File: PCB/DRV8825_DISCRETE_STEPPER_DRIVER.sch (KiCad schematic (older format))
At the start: 13 parts, among them U2 DRV8825PWPR

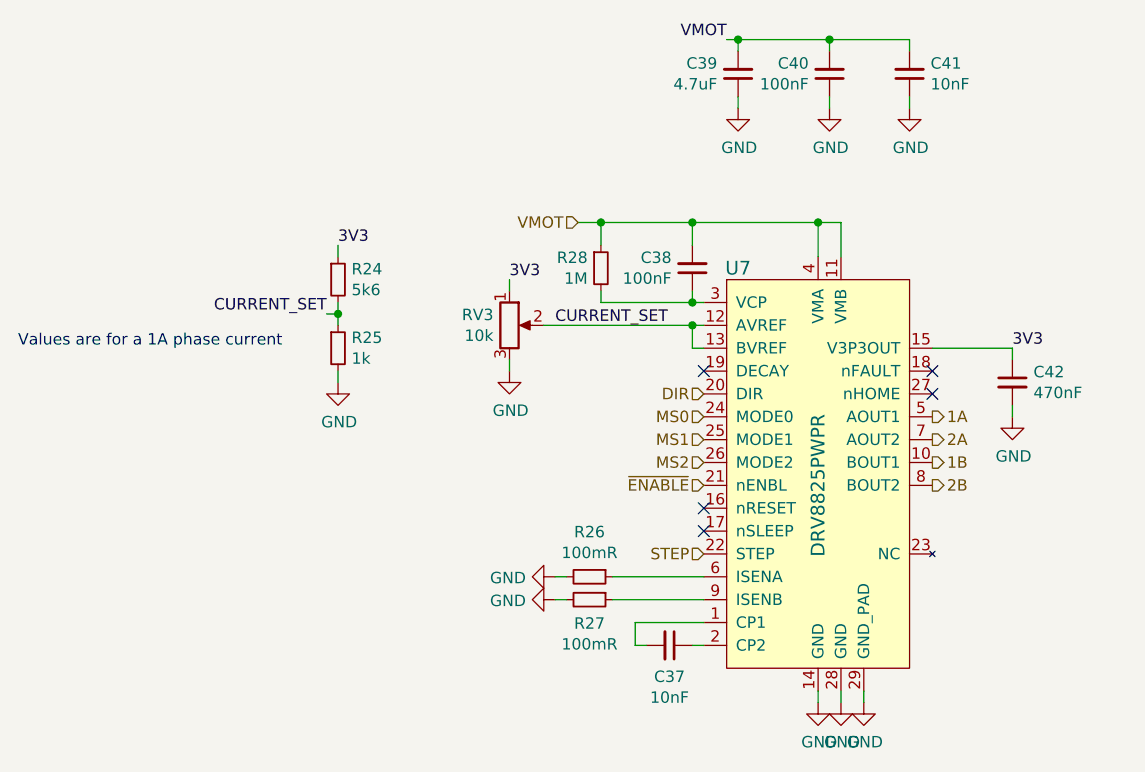
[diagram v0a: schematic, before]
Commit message: Added correct DRV breakout and added testpoints
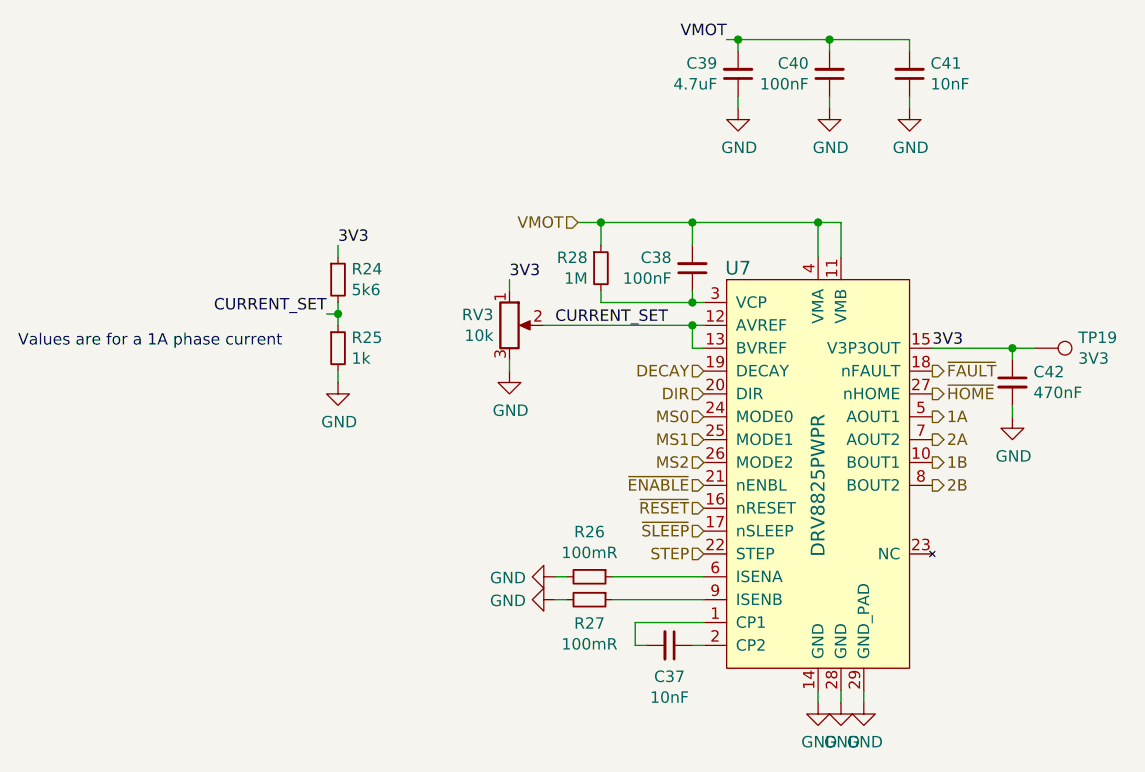
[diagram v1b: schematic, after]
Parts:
- added TP7: 3V3, symbol Connector:TestPoint
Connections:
- net 3V3: now also TP7.1
- net ~RESET: now reaches U2.16 (nRESET)
- net ~SLEEP: now reaches U2.17 (nSLEEP)
- net ~FAULT: now reaches U2.18 (nFAULT)
- net DECAY: now reaches U2.19 (DECAY)
- net ~HOME: now reaches U2.27 (nHOME)
- no-connect marks 5 -> 0
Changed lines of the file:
@@
 Text HLabel 5150 4150 0    50   Input ~ 0
 ~ENABLE
-NoConn ~ 5150 4250
-NoConn ~ 5150 4350
 Text HLabel 5150 3750 0    50   Input ~ 0
 DIR
-NoConn ~ 5150 3650
 $Comp
 L Device:R_POT RV1
@@
 Wire Wire Line
 	5650 5050 5650 5100
-NoConn ~ 6150 3650
-NoConn ~ 6150 3750
 $Comp
 L Device:C_Small C15
@@
 Text Label 4300 3250 0    50   ~ 0
 3V3
-Text Label 6500 3550 0    50   ~ 0
+Text Label 6150 3550 0    50   ~ 0
 3V3
 Text Label 4500 3450 0    50   ~ 0
@@
 Text HLabel 5150 4050 0    50   Input ~ 0
 MS2
+Text HLabel 5150 4350 0    50   Input ~ 0
+~SLEEP
+Text HLabel 5150 4250 0    50   Input ~ 0
+~RESET
+Text HLabel 6150 3650 2    50   Output ~ 0
+~FAULT
+Text HLabel 6150 3750 2    50   Output ~ 0
+~HOME
+$Comp
+L Connector:TestPoint TP?
+U 1 1 5E958C53
+P 6600 3550
+AR Path="/5E958C53" Ref="TP?"  Part="1"
+AR Path="/5E8A6686/5E8D27A6/5E958C53" Ref="TP7"  Part="1"
+AR Path="/5E8813FF/5E8D27A6/5E958C53" Ref="TP19"  Part="1"
+F 0 "TP19" V 6554 3738 50  0000 L CNN
+F 1 "3V3" V 6645 3738 50  0000 L CNN
+F 2 "" H 6800 3550 50  0001 C CNN
+F 3 "~" H 6800 3550 50  0001 C CNN
+	1    6600 3550
+	0    1    1    0
+$EndComp
+Wire Wire Line
+	6600 3550 6500 3550
+Connection ~ 6500 3550
+Text HLabel 5150 3650 0    50   Input ~ 0
+DECAY
 $EndSCHEMATC

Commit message: Added remaining test points
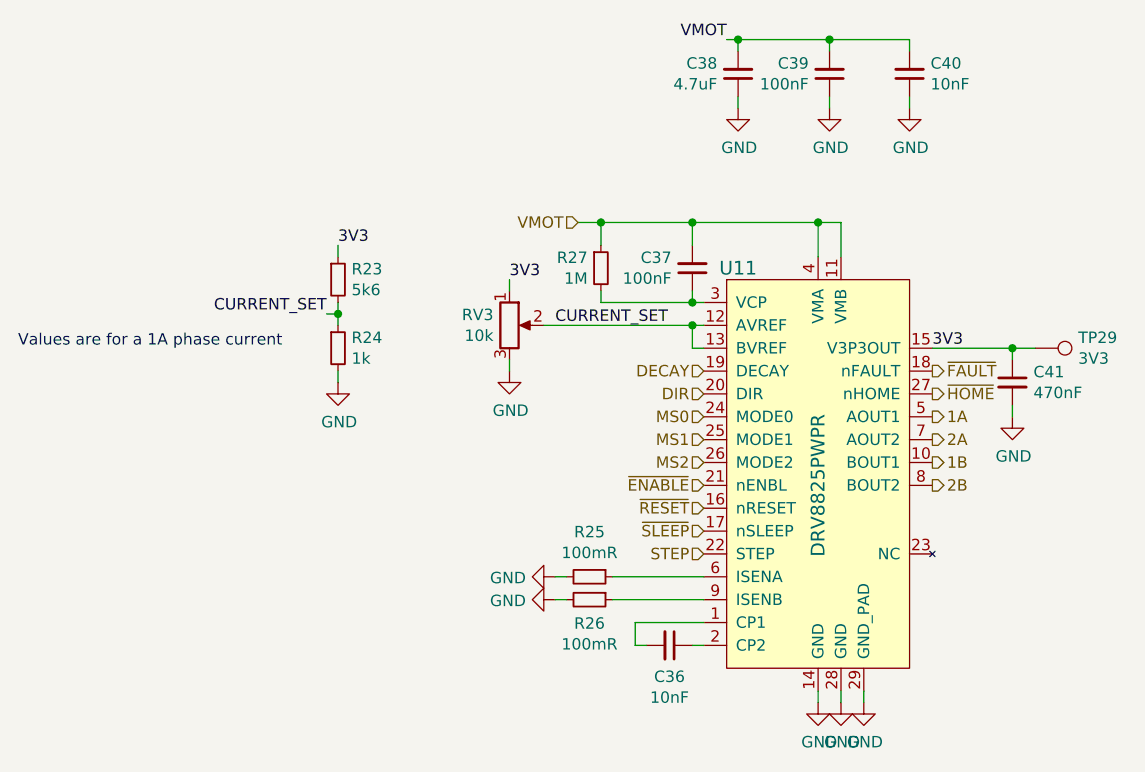
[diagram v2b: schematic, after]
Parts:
- renumbered C13 to C11, C14 to C12, C15 to C13, C16 to C14, C17 to C15, C18 to C16, TP7 to TP11, U2 to U4

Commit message: Added breakout footprints
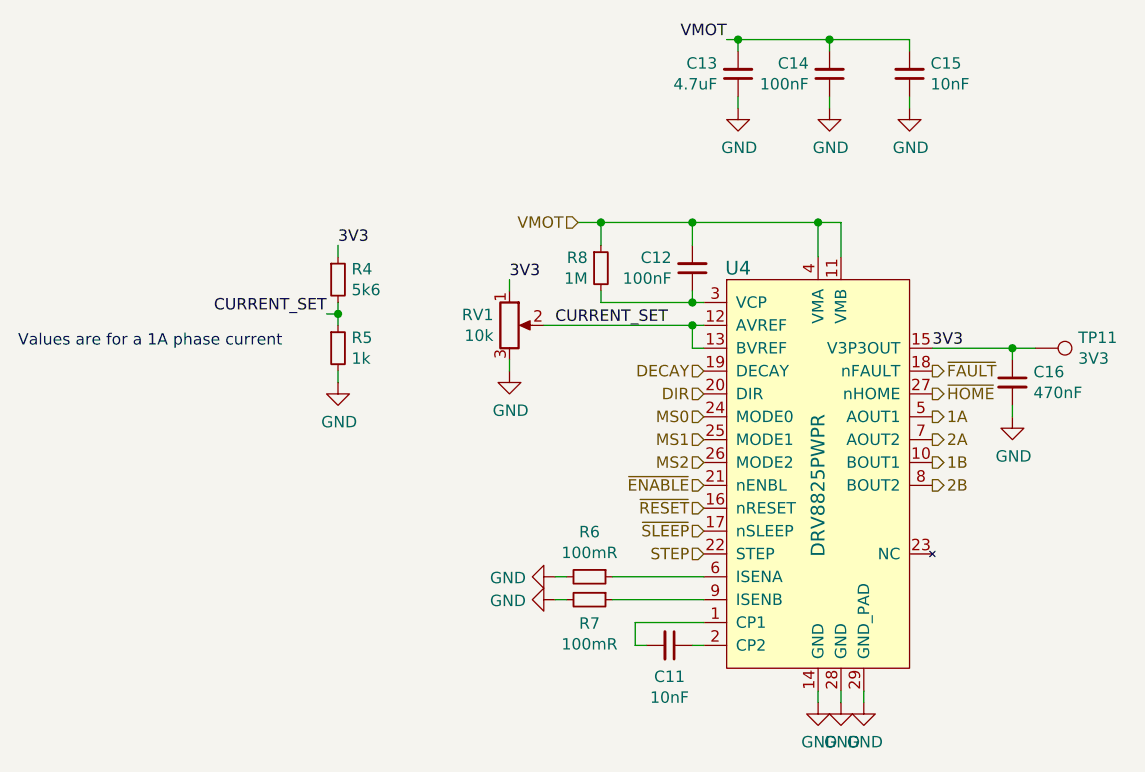
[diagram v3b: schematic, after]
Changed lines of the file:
@@
 AR Path="/5E8A6686/5E8D27A6/5E8D3351" Ref="U4"  Part="1"
 AR Path="/5E8813FF/5E8D27A6/5E8D3351" Ref="U11"  Part="1"
-F 0 "U11" H 5300 4500 60  0000 C CNN
+F 0 "U4" H 5300 4500 60  0000 C CNN
 F 1 "DRV8825PWPR" V 5650 3550 60  0000 C CNN
 F 2 "digikey-footprints:TSSOP-28-1EP_W4.40mm" H 5750 4050 60  0001 L CNN
@@
 AR Path="/5E8A6686/5E8D27A6/5E8D575F" Ref="C11"  Part="1"
 AR Path="/5E8813FF/5E8D27A6/5E8D575F" Ref="C36"  Part="1"
-F 0 "C36" V 5137 4850 50  0000 C CNN
+F 0 "C11" V 5137 4850 50  0000 C CNN
 F 1 "10nF" V 5228 4850 50  0000 C CNN
 F 2 "" H 5000 4850 50  0001 C CNN
@@
 AR Path="/5E8A6686/5E8D27A6/5E8D7A25" Ref="R6"  Part="1"
 AR Path="/5E8813FF/5E8D27A6/5E8D7A25" Ref="R25"  Part="1"
-F 0 "R25" V 4454 4550 50  0000 C CNN
+F 0 "R6" V 4454 4550 50  0000 C CNN
 F 1 "100mR" V 4545 4550 50  0000 C CNN
 F 2 "" H 4650 4550 50  0001 C CNN
@@
 AR Path="/5E8A6686/5E8D27A6/5E8D7F7E" Ref="R7"  Part="1"
 AR Path="/5E8813FF/5E8D27A6/5E8D7F7E" Ref="R26"  Part="1"
-F 0 "R26" V 4754 4650 50  0000 C CNN
+F 0 "R7" V 4754 4650 50  0000 C CNN
 F 1 "100mR" V 4845 4650 50  0000 C CNN
 F 2 "" H 4650 4650 50  0001 C CNN
@@
 AR Path="/5E8A6686/5E8D27A6/5E8DA337" Ref="C12"  Part="1"
 AR Path="/5E8813FF/5E8D27A6/5E8DA337" Ref="C37"  Part="1"
-F 0 "C37" H 5191 3154 50  0000 L CNN
+F 0 "C12" H 5191 3154 50  0000 L CNN
 F 1 "100nF" H 5191 3245 50  0000 L CNN
 F 2 "" H 5100 3200 50  0001 C CNN
@@
 AR Path="/5E8A6686/5E8D27A6/5E8DF1FC" Ref="RV1"  Part="1"
 AR Path="/5E8813FF/5E8D27A6/5E8DF1FC" Ref="RV3"  Part="1"
-F 0 "RV3" H 4230 3496 50  0000 R CNN
+F 0 "RV1" H 4230 3496 50  0000 R CNN
 F 1 "10k" H 4230 3405 50  0000 R CNN
 F 2 "" H 4300 3450 50  0001 C CNN
@@
 AR Path="/5E8A6686/5E8D27A6/5E8E181B" Ref="C16"  Part="1"
 AR Path="/5E8813FF/5E8D27A6/5E8E181B" Ref="C41"  Part="1"
-F 0 "C41" H 6592 3746 50  0000 L CNN
+F 0 "C16" H 6592 3746 50  0000 L CNN
 F 1 "470nF" H 6592 3655 50  0000 L CNN
 F 2 "" H 6500 3700 50  0001 C CNN
@@
 AR Path="/5E8A6686/5E8D27A6/5E8E9760" Ref="C13"  Part="1"
 AR Path="/5E8813FF/5E8D27A6/5E8E9760" Ref="C38"  Part="1"
-F 0 "C38" H 5391 2304 50  0000 L CNN
+F 0 "C13" H 5391 2304 50  0000 L CNN
 F 1 "4.7uF" H 5391 2395 50  0000 L CNN
 F 2 "" H 5300 2350 50  0001 C CNN
@@
 AR Path="/5E8A6686/5E8D27A6/5E8E999E" Ref="C14"  Part="1"
 AR Path="/5E8813FF/5E8D27A6/5E8E999E" Ref="C39"  Part="1"
-F 0 "C39" H 5791 2304 50  0000 L CNN
+F 0 "C14" H 5791 2304 50  0000 L CNN
 F 1 "100nF" H 5791 2395 50  0000 L CNN
 F 2 "" H 5700 2350 50  0001 C CNN
@@
 AR Path="/5E8A6686/5E8D27A6/5E8E9DB5" Ref="C15"  Part="1"
 AR Path="/5E8813FF/5E8D27A6/5E8E9DB5" Ref="C40"  Part="1"
-F 0 "C40" H 5958 2304 50  0000 R CNN
+F 0 "C15" H 5958 2304 50  0000 R CNN
 F 1 "10nF" H 5958 2395 50  0000 R CNN
 F 2 "" H 6050 2350 50  0001 C CNN
@@
 AR Path="/5E8A6686/5E8D27A6/5E8B797B" Ref="R4"  Part="1"
 AR Path="/5E8813FF/5E8D27A6/5E8B797B" Ref="R23"  Part="1"
-F 0 "R23" H 3609 3296 50  0000 L CNN
+F 0 "R4" H 3609 3296 50  0000 L CNN
 F 1 "5k6" H 3609 3205 50  0000 L CNN
 F 2 "" H 3550 3250 50  0001 C CNN
@@
 AR Path="/5E8A6686/5E8D27A6/5E8B7AF6" Ref="R5"  Part="1"
 AR Path="/5E8813FF/5E8D27A6/5E8B7AF6" Ref="R24"  Part="1"
-F 0 "R24" H 3609 3596 50  0000 L CNN
+F 0 "R5" H 3609 3596 50  0000 L CNN
 F 1 "1k" H 3609 3505 50  0000 L CNN
 F 2 "" H 3550 3550 50  0001 C CNN
@@
 AR Path="/5E8A6686/5E8D27A6/5E8D6554" Ref="R8"  Part="1"
 AR Path="/5E8813FF/5E8D27A6/5E8D6554" Ref="R27"  Part="1"
-F 0 "R27" H 4642 3246 50  0000 R CNN
+F 0 "R8" H 4642 3246 50  0000 R CNN
 F 1 "1M" H 4642 3155 50  0000 R CNN
 F 2 "" H 4700 3200 50  0001 C CNN
@@
 AR Path="/5E8A6686/5E8D27A6/5E958C53" Ref="TP11"  Part="1"
 AR Path="/5E8813FF/5E8D27A6/5E958C53" Ref="TP29"  Part="1"
-F 0 "TP29" V 6554 3738 50  0000 L CNN
+F 0 "TP11" V 6554 3738 50  0000 L CNN
 F 1 "3V3" V 6645 3738 50  0000 L CNN
 F 2 "" H 6800 3550 50  0001 C CNN
